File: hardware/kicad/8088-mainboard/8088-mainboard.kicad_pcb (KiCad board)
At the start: 2 copper layers, 170 x 125 mm, 47 parts, among them J1 Conn_01x10, J2 Exp0, J3 Exp1, J4 POWER 5v, J5 Ext CLK, Q1 NDP6020P, SW1 Reset, SW2 SW_DIP_x02, U1 8088_Min_Mode, U2 74LS373, U3 74LS373, U4 74LS245, U5 8284, U6 74LS138, U7 74LS138, U8 28C256, U9 HM62256BLP, Y1 14.31818 MHz

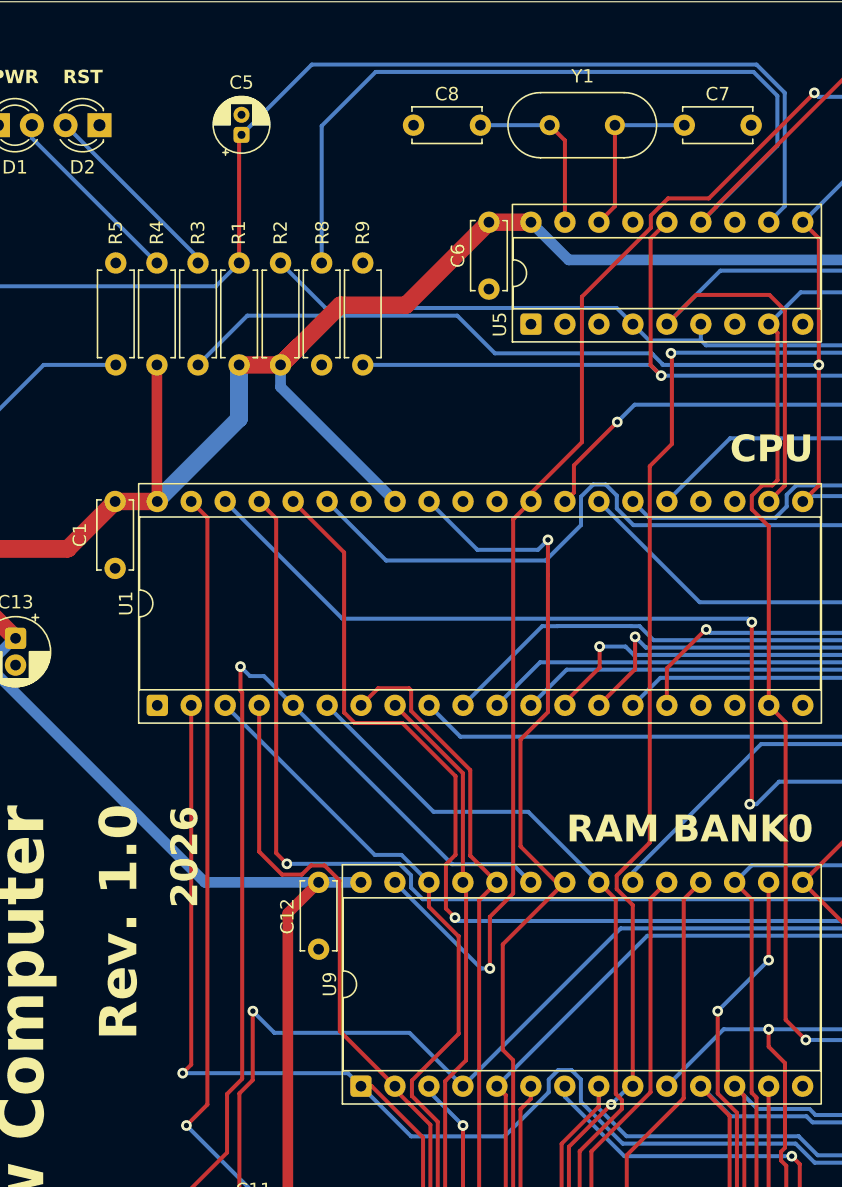
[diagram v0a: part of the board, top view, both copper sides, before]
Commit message: Add LCD module and demo BIOS
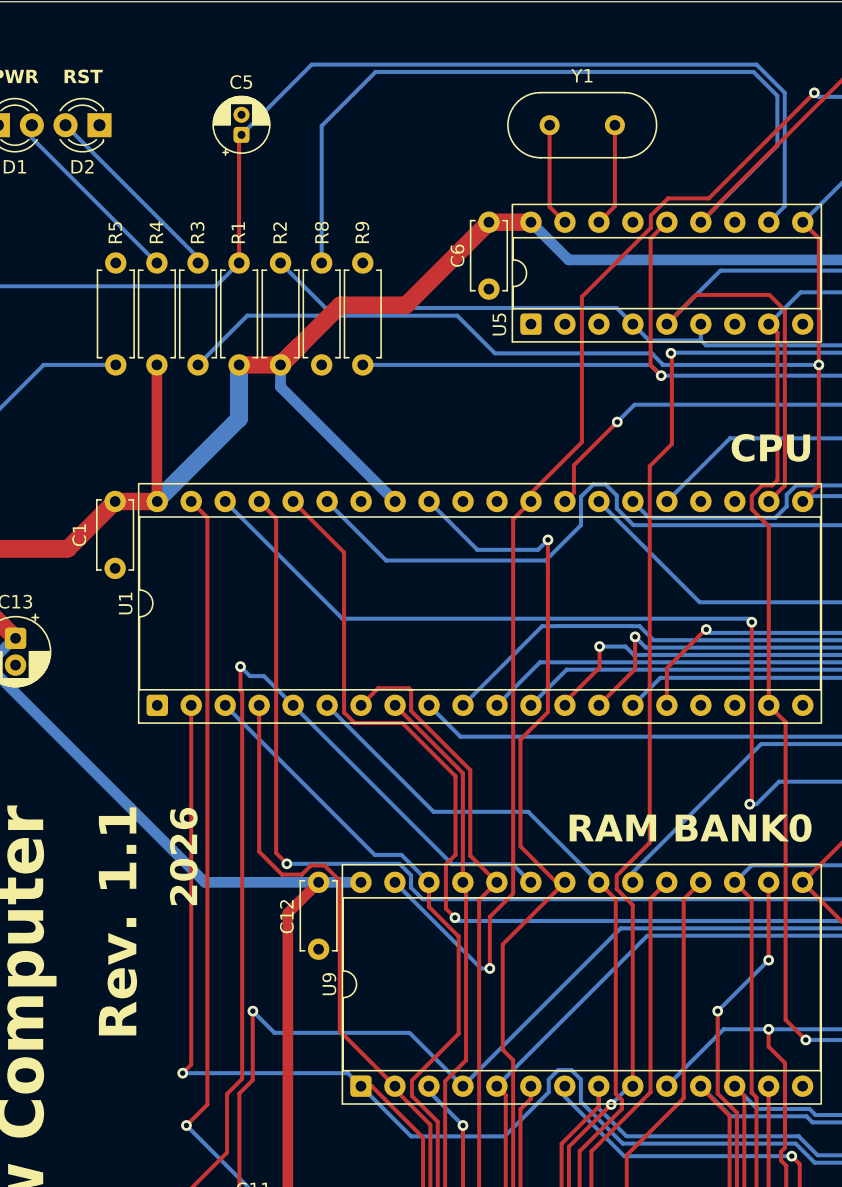
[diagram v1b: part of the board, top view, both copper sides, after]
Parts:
- removed C7, C8: 33 pF, Capacitor_THT:C_Disc_D5.0mm_W2.5mm_P5.00mm
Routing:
- net Net-(U5-X2): track 12.9 -> 7.75 mm
- net Net-(U5-X1): track 12.9 -> 7.73 mm
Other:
- board text added: "Rev. 1.1"
- board text removed: "Rev. 1.0"
